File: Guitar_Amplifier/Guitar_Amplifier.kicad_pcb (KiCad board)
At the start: 2 copper layers, 39 x 16 mm, 11 parts, among them J1 Conn_01x04, J2 Conn_01x02, U1 LM386

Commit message: Created gerbers, Added GND copper pour
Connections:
- net Net-(C3-Pad1) renamed /Vout
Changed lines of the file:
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@@
 	(paper "A4")
 	(layers
-		(0 "F.Cu" signal)
+		(0 "F.Cu" signal "T.Cu")
 		(31 "B.Cu" signal)
-		(32 "B.Adhes" user "B.Adhesive")
-		(33 "F.Adhes" user "F.Adhesive")
 		(34 "B.Paste" user)
 		(35 "F.Paste" user)
@@
 		(38 "B.Mask" user)
 		(39 "F.Mask" user)
-		(40 "Dwgs.User" user "User.Drawings")
-		(41 "Cmts.User" user "User.Comments")
-		(42 "Eco1.User" user "User.Eco1")
-		(43 "Eco2.User" user "User.Eco2")
 		(44 "Edge.Cuts" user)
 		(45 "Margin" user)
@@
 		(47 "F.CrtYd" user "F.Courtyard")
 		(48 "B.Fab" user)
-		(49 "F.Fab" user)
-		(50 "User.1" user)
-		(51 "User.2" user)
-		(52 "User.3" user)
-		(53 "User.4" user)
-		(54 "User.5" user)
-		(55 "User.6" user)
-		(56 "User.7" user)
-		(57 "User.8" user)
 		(58 "User.9" user)
 	)
 	(setup
+		(stackup
+			(layer "F.SilkS"
+				(type "Top Silk Screen")
+			)
+			(layer "F.Paste"
+				(type "Top Solder Paste")
+			)
+			(layer "F.Mask"
+				(type "Top Solder Mask")
+				(thickness 0.01)
+			)
+			(layer "F.Cu"
+				(type "copper")
+				(thickness 0.035)
+			)
+			(layer "dielectric 1"
+				(type "core")
+				(thickness 1.51)
+				(material "FR4")
+				(epsilon_r 4.5)
+				(loss_tangent 0.02)
+			)
+			(layer "B.Cu"
+				(type "copper")
+				(thickness 0.035)
+			)
+			(layer "B.Mask"
+				(type "Bottom Solder Mask")
+				(thickness 0.01)
+			)
+			(layer "B.Paste"
+				(type "Bottom Solder Paste")
+			)
+			(layer "B.SilkS"
+				(type "Bottom Silk Screen")
+			)
+			(copper_finish "None")
+			(dielectric_constraints no)
+		)
 		(pad_to_mask_clearance 0)
 		(allow_soldermask_bridges_in_footprints no)
@@
 			(psa4output no)
 			(plotreference yes)
-			(plotvalue yes)
+			(plotvalue no)
 			(plotfptext yes)
 			(plotinvisibletext no)
@@
 			(outputformat 1)
 			(mirror no)
-			(drillshape 1)
+			(drillshape 0)
 			(scaleselection 1)
-			(outputdirectory "")
+			(outputdirectory "gerbers/")
 		)
 	)
@@
 	(net 3 "Net-(C2-Pad2)")
 	(net 4 "Net-(C2-Pad1)")
-	(net 5 "Net-(C3-Pad1)")
-	(net 6 "Net-(J2-Pin_1)")
-	(net 7 "Net-(C4-Pad1)")
-	(net 8 "Net-(D1-A)")
-	(net 9 "Net-(J1-Pin_2)")
-	(net 10 "Net-(U1-+)")
-	(net 11 "unconnected-(U1-BYPASS-Pad7)")
+	(net 5 "Net-(J2-Pin_1)")
+	(net 6 "Net-(C4-Pad1)")
+	(net 7 "Net-(D1-A)")
+	(net 8 "Net-(J1-Pin_2)")
+	(net 9 "Net-(U1-+)")
+	(net 10 "unconnected-(U1-BYPASS-Pad7)")
+	(net 11 "/Vout")
 	(footprint "Capacitor_SMD:CP_Elec_10x10"
 		(layer "F.Cu")
@@
 			(layers "F.Cu" "F.Paste" "F.Mask")
 			(roundrect_rratio 0.1)
-			(net 5 "Net-(C3-Pad1)")
+			(net 11 "/Vout")
 			(pintype "passive")
 		)
@@
 			(layers "F.Cu" "F.Paste" "F.Mask")
 			(roundrect_rratio 0.1)
-			(net 6 "Net-(J2-Pin_1)")
+			(net 5 "Net-(J2-Pin_1)")
 			(pintype "passive")
 		)
@@
 			(layers "*.Cu" "*.Mask")
 			(remove_unused_layers no)
-			(net 9 "Net-(J1-Pin_2)")
+			(net 8 "Net-(J1-Pin_2)")
 			(pinfunction "Pin_2")
 			(pintype "passive")
@@
 			(layers "F.Cu" "F.Paste" "F.Mask")
 			(roundrect_rratio 0.25)
-			(net 8 "Net-(D1-A)")
+			(net 7 "Net-(D1-A)")
 			(pinfunction "A")
 			(pintype "passive")
@@
 			(size 1.2 1.2)
 			(layers "F.Cu" "F.Paste" "F.Mask")
-			(net 9 "Net-(J1-Pin_2)")
+			(net 8 "Net-(J1-Pin_2)")
 			(pinfunction "1")
 			(pintype "passive")
@@
 			(size 1.5 1.6)
 			(layers "F.Cu" "F.Paste" "F.Mask")
-			(net 10 "Net-(U1-+)")
+			(net 9 "Net-(U1-+)")
 			(pinfunction "2")
 			(pintype "passive")
@@
 			(layers "F.Cu" "F.Paste" "F.Mask")
 			(roundrect_rratio 0.25)
-			(net 8 "Net-(D1-A)")
+			(net 7 "Net-(D1-A)")
 			(pintype "passive")
 		)
@@
 			(layers "F.Cu" "F.Paste" "F.Mask")
 			(roundrect_rratio 0.25)
-			(net 10 "Net-(U1-+)")
+			(net 9 "Net-(U1-+)")
 			(pinfunction "+")
 			(pintype "input")
@@
 			(layers "F.Cu" "F.Paste" "F.Mask")
 			(roundrect_rratio 0.25)
-			(net 5 "Net-(C3-Pad1)")
+			(net 11 "/Vout")
 			(pintype "output")
 		)
@@
 			(layers "F.Cu" "F.Paste" "F.Mask")
 			(roundrect_rratio 0.25)
-			(net 11 "unconnected-(U1-BYPASS-Pad7)")
+			(net 10 "unconnected-(U1-BYPASS-Pad7)")
 			(pinfunction "BYPASS")
 			(pintype "input+no_connect")
@@
 			(layers "*.Cu" "*.Mask")
 			(remove_unused_layers no)
-			(net 6 "Net-(J2-Pin_1)")
+			(net 5 "Net-(J2-Pin_1)")
 			(pinfunction "Pin_1")
 			(pintype "passive")
@@
 			(layers "F.Cu" "F.Paste" "F.Mask")
 			(roundrect_rratio 0.25)
-			(net 7 "Net-(C4-Pad1)")
+			(net 6 "Net-(C4-Pad1)")
 			(pintype "passive")
 		)
@@
 			(layers "F.Cu" "F.Paste" "F.Mask")
 			(roundrect_rratio 0.25)
-			(net 5 "Net-(C3-Pad1)")
+			(net 11 "/Vout")
 			(pintype "passive")
 		)
@@
 			(layers "F.Cu" "F.Paste" "F.Mask")
 			(roundrect_rratio 0.25)
-			(net 7 "Net-(C4-Pad1)")
+			(net 6 "Net-(C4-Pad1)")
 			(pintype "passive")
 		)
@@
 		(start 108 76)
 		(end 147 92)
+		(locked yes)
 		(stroke
 			(width 0.2)
@@
 	)
 	(segment
-		(start 129.5 84)
-		(end 132 84)
+		(start 144 84)
+		(end 144.5 84.5)
 		(width 0.2)
 		(layer "F.Cu")
@@
 	)
 	(segment
-		(start 127.5 87.725)
-		(end 127.5 86)
+		(start 140 84)
+		(end 144 84)
 		(width 0.2)
 		(layer "F.Cu")
@@
 	)
 	(segment
-		(start 127.5 86)
-		(end 129.5 84)
+		(start 127.5 89.275)
+		(end 129.45 89.275)
 		(width 0.2)
 		(layer "F.Cu")
-		(net 5)
+		(net 6)
 	)
 	(segment
-		(start 127.18 87.405)
-		(end 127.5 87.725)
+		(start 129.45 89.275)
+		(end 129.5 89.325)
 		(width 0.2)
 		(layer "F.Cu")
-		(net 5)
+		(net 6)
 	)
 	(segment
-		(start 124.475 87.405)
-		(end 127.18 87.405)
+		(start 113.7625 81.5)
+		(end 115.5225 81.5)
 		(width 0.2)
 		(layer "F.Cu")
-		(net 5)
+		(net 7)
 	)
 	(segment
-		(start 144 84)
-		(end 144.5 84.5)
+		(start 112.2 84.5)
+		(end 110 84.5)
 		(width 0.2)
 		(layer "F.Cu")
-		(net 6)
+		(net 8)
 	)
 	(segment
-		(start 140 84)
-		(end 144 84)
+		(start 112.7 85)
+		(end 112.2 84.5)
 		(width 0.2)
 		(layer "F.Cu")
-		(net 6)
+		(net 8)
 	)
 	(segment
-		(start 127.5 89.275)
-		(end 129.45 89.275)
+		(start 115.95 86)
+		(end 119.39 86)
 		(width 0.2)
 		(layer "F.Cu")
-		(net 7)
+		(net 9)
 	)
 	(segment
-		(start 129.45 89.275)
-		(end 129.5 89.325)
+		(start 119.39 86)
+		(end 119.525 86.135)
 		(width 0.2)
 		(layer "F.Cu")
-		(net 7)
+		(net 9)
 	)
 	(segment
-		(start 113.7625 81.5)
-		(end 115.5225 81.5)
+		(start 129.5 84)
+		(end 132 84)
 		(width 0.2)
 		(layer "F.Cu")
-		(net 8)
+		(net 11)
 	)
 	(segment
-		(start 112.2 84.5)
-		(end 110 84.5)
+		(start 127.5 87.725)
+		(end 127.5 86)
 		(width 0.2)
 		(layer "F.Cu")
-		(net 9)
+		(net 11)
 	)
 	(segment
-		(start 112.7 85)
-		(end 112.2 84.5)
+		(start 127.5 86)
+		(end 129.5 84)
 		(width 0.2)
 		(layer "F.Cu")
-		(net 9)
+		(net 11)
 	)
 	(segment
-		(start 115.95 86)
-		(end 119.39 86)
+		(start 127.18 87.405)
+		(end 127.5 87.725)
 		(width 0.2)
 		(layer "F.Cu")
-		(net 10)
+		(net 11)
 	)
 	(segment
-		(start 119.39 86)
-		(end 119.525 86.135)
+		(start 124.475 87.405)
+		(end 127.18 87.405)
 		(width 0.2)
 		(layer "F.Cu")
-		(net 10)
+		(net 11)
 	)
 	(zone
@@
 		(net_name "GND")
 		(layer "B.Cu")
-		(hatch edge 0.5)
+		(name "gnd")
+		(hatch none 0.5)
 		(connect_pads
 			(clearance 0.5)
@@
 		(min_thickness 0.25)
 		(filled_areas_thickness no)
-		(fill
+		(fill yes
 			(thermal_gap 0.5)
 			(thermal_bridge_width 0.5)
@@
 		(polygon
 			(pts
-				(xy 108.5 76.5) (xy 146.5 76.5) (xy 146.5 91.5) (xy 108.5 91.5)
+				(xy 108.5 91.5) (xy 108.5 76.5) (xy 146.5 76.5) (xy 146.5 91.5)
 			)
 		)

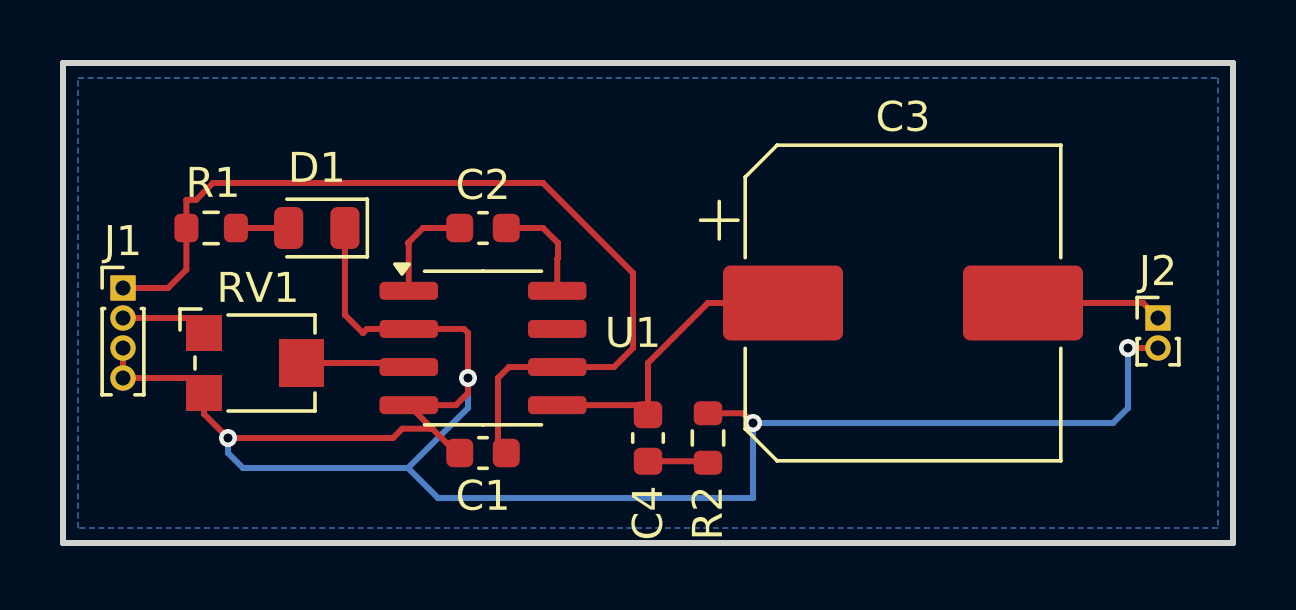
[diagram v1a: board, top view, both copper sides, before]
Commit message: Added 3PDT Switch
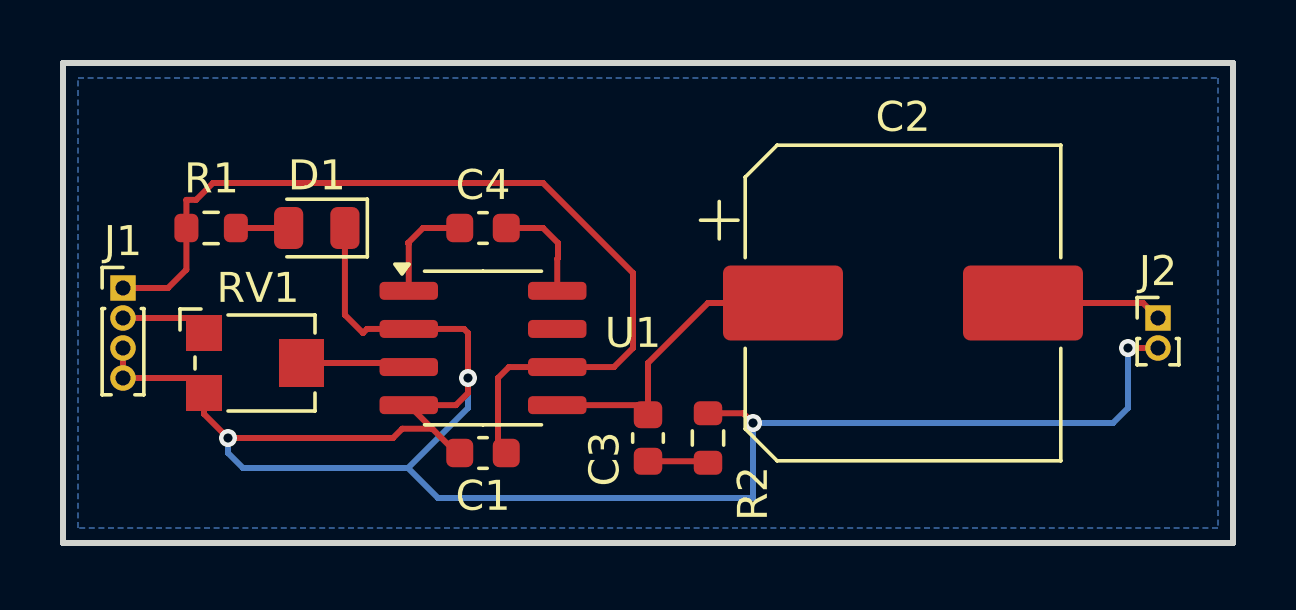
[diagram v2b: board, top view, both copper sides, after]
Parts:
- renumbered C3 to C2, C4 to C3, C2 to C4
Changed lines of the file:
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@@
 	(net 1 "GND")
 	(net 2 "+9V")
-	(net 3 "Net-(C2-Pad2)")
-	(net 4 "Net-(C2-Pad1)")
+	(net 3 "Net-(C3-Pad1)")
+	(net 4 "Net-(C4-Pad2)")
 	(net 5 "Net-(J2-Pin_1)")
 	(net 6 "Net-(C4-Pad1)")
@@
 		(descr "SMD capacitor, aluminum electrolytic, Nichicon, 10.0x10.0mm")
 		(tags "capacitor electrolytic")
-		(property "Reference" "C3"
+		(property "Reference" "C2"
 			(at 0 -6.2 0)
 			(layer "F.SilkS")
@@
 		(tags "diode")
 		(property "Reference" "D1"
-			(at 0 2 180)
+			(at 0 1.75 180)
 			(layer "F.SilkS")
 			(effects
@@
 		(tags "resistor")
 		(property "Reference" "R1"
-			(at 0.0625 -1.5 0)
+			(at 0.0125 -1.65 0)
 			(layer "F.SilkS")
 			(effects
@@
 			(layers "F.Cu" "F.Paste" "F.Mask")
 			(roundrect_rratio 0.25)
-			(net 4 "Net-(C2-Pad1)")
+			(net 6 "Net-(C4-Pad1)")
 			(pinfunction "GAIN")
 			(pintype "input")
@@
 			(layers "F.Cu" "F.Paste" "F.Mask")
 			(roundrect_rratio 0.25)
-			(net 3 "Net-(C2-Pad2)")
+			(net 4 "Net-(C4-Pad2)")
 			(pinfunction "GAIN")
 			(pintype "input")
@@
 		(descr "Capacitor SMD 0603 (1608 Metric), square (rectangular) end terminal, IPC_7351 nominal, (Body size source: IPC-SM-782 page 76, https://www.pcb-3d.com/wordpress/wp-content/uploads/ipc-sm-782a_amendment_1_and_2.pdf), generated with kicad-footprint-generator")
 		(tags "capacitor")
-		(property "Reference" "C4"
-			(at -2.5 0 270)
+		(property "Reference" "C3"
+			(at -0.7 -1.45 -90)
 			(layer "F.SilkS")
 			(effects
@@
 		)
 		(property "Value" "47nF"
-			(at 0 1.43 270)
+			(at 0 1.43 -90)
 			(layer "F.Fab")
 			(hide yes)
@@
 		)
 		(fp_text user "${REFERENCE}"
-			(at 0 0 270)
+			(at 0 0 -90)
 			(layer "F.Fab")
 			(effects
@@
 			(layers "F.Cu" "F.Paste" "F.Mask")
 			(roundrect_rratio 0.25)
-			(net 6 "Net-(C4-Pad1)")
+			(net 3 "Net-(C3-Pad1)")
 			(pintype "passive")
 		)
@@
 		(descr "Capacitor SMD 0603 (1608 Metric), square (rectangular) end terminal, IPC_7351 nominal, (Body size source: IPC-SM-782 page 76, https://www.pcb-3d.com/wordpress/wp-content/uploads/ipc-sm-782a_amendment_1_and_2.pdf), generated with kicad-footprint-generator")
 		(tags "capacitor")
-		(property "Reference" "C2"
+		(property "Reference" "C4"
 			(at 0 -1.43 0)
 			(layer "F.SilkS")
@@
 			(layers "F.Cu" "F.Paste" "F.Mask")
 			(roundrect_rratio 0.25)
-			(net 4 "Net-(C2-Pad1)")
+			(net 6 "Net-(C4-Pad1)")
 			(pintype "passive")
 		)
@@
 			(layers "F.Cu" "F.Paste" "F.Mask")
 			(roundrect_rratio 0.25)
-			(net 3 "Net-(C2-Pad2)")
+			(net 4 "Net-(C4-Pad2)")
 			(pintype "passive")
 		)
@@
 		(tags "resistor")
 		(property "Reference" "R2"
-			(at -2.5 0 270)
+			(at -1.85 1.5 -90)
 			(layer "F.SilkS")
 			(effects
@@
 		)
 		(property "Value" "10"
-			(at 0 1.43 270)
+			(at 0 1.43 -90)
 			(layer "F.Fab")
 			(hide yes)
@@
 		)
 		(fp_text user "${REFERENCE}"
-			(at 0 0 270)
+			(at 0 0 -90)
 			(layer "F.Fab")
 			(effects
@@
 			(layers "F.Cu" "F.Paste" "F.Mask")
 			(roundrect_rratio 0.25)
-			(net 6 "Net-(C4-Pad1)")
+			(net 3 "Net-(C3-Pad1)")
 			(pintype "passive")
 		)
@@
 	)
 	(segment
-		(start 124.5 82.5)
-		(end 124.475 82.525)
-		(width 0.2)
-		(layer "F.Cu")
-		(net 3)
-	)
-	(segment
-		(start 124.475 82.525)
-		(end 124.475 83.595)
-		(width 0.2)
-		(layer "F.Cu")
-		(net 3)
-	)
-	(segment
-		(start 122.775 81.5)
-		(end 124 81.5)
+		(start 127.5 89.275)
+		(end 129.45 89.275)
 		(width 0.2)
 		(layer "F.Cu")
@@
 	)
 	(segment
-		(start 124.5 82)
-		(end 124.5 82.5)
+		(start 129.45 89.275)
+		(end 129.5 89.325)
 		(width 0.2)
 		(layer "F.Cu")
@@
 	)
 	(segment
-		(start 124 81.5)
-		(end 124.5 82)
+		(start 124.5 82.5)
+		(end 124.475 82.525)
 		(width 0.2)
 		(layer "F.Cu")
-		(net 3)
+		(net 4)
 	)
 	(segment
-		(start 119.5 82)
-		(end 120 81.5)
+		(start 124.475 82.525)
+		(end 124.475 83.595)
 		(width 0.2)
 		(layer "F.Cu")
@@
 	)
 	(segment
-		(start 119.525 82.025)
-		(end 119.5 82)
+		(start 122.775 81.5)
+		(end 124 81.5)
 		(width 0.2)
 		(layer "F.Cu")
@@
 	)
 	(segment
-		(start 119.525 83.595)
-		(end 119.525 82.025)
+		(start 124.5 82)
+		(end 124.5 82.5)
 		(width 0.2)
 		(layer "F.Cu")
@@
 	)
 	(segment
-		(start 120 81.5)
-		(end 121.225 81.5)
+		(start 124 81.5)
+		(end 124.5 82)
 		(width 0.2)
 		(layer "F.Cu")
@@
 	)
 	(segment
-		(start 127.5 89.275)
-		(end 129.45 89.275)
+		(start 119.5 82)
+		(end 120 81.5)
 		(width 0.2)
 		(layer "F.Cu")
@@
 	)
 	(segment
-		(start 129.45 89.275)
-		(end 129.5 89.325)
+		(start 119.525 82.025)
+		(end 119.5 82)
+		(width 0.2)
+		(layer "F.Cu")
+		(net 6)
+	)
+	(segment
+		(start 119.525 83.595)
+		(end 119.525 82.025)
+		(width 0.2)
+		(layer "F.Cu")
+		(net 6)
+	)
+	(segment
+		(start 120 81.5)
+		(end 121.225 81.5)
 		(width 0.2)
 		(layer "F.Cu")
